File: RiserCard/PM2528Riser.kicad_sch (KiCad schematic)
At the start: 63 parts, among them K2 Conn_02x40_Odd_Even

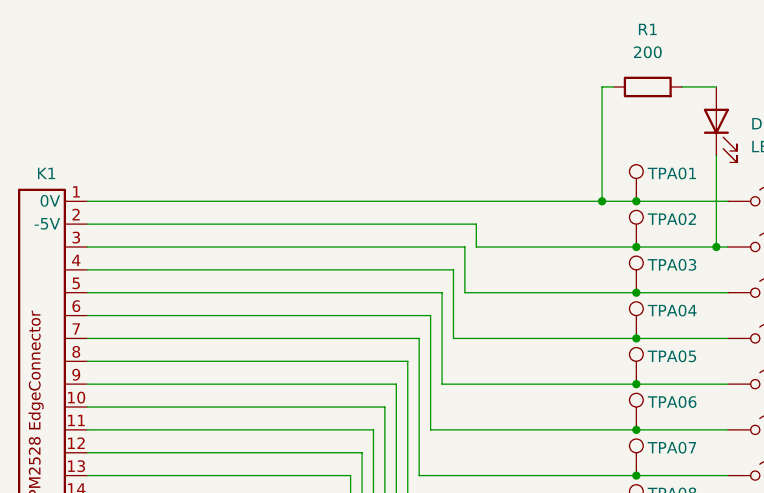
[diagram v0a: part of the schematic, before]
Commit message: Replaced testpins with testloops/beads
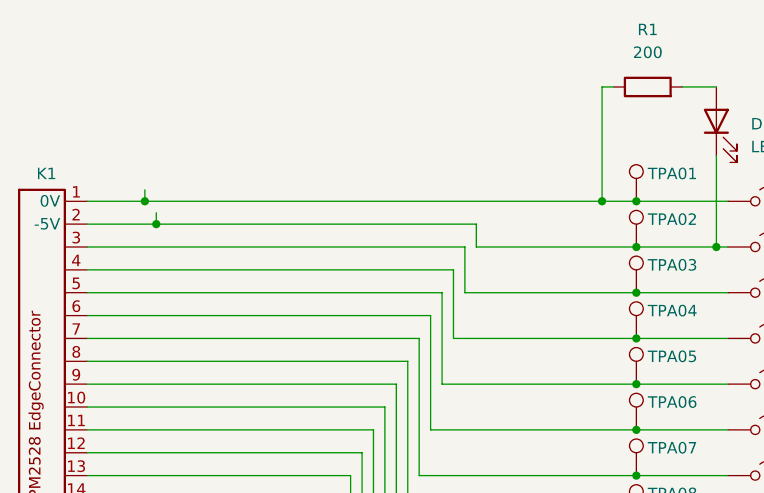
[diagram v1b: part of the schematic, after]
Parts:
- K1: symbol _PhilipsPM2528DMM:PCBEdge_Plugincard -> PM2528:PCBEdge_Plugincard
- TPB01, TPB02, TPB03, TPB04, TPB05, TPB06, TPB07, TPB08, TPB09, TPB10, TPB11, TPB12, TPB13, TPB14, TPB15, TPB16, TPB17, TPB18, TPB19: footprint Pin_D1.0mm_L10.0mm -> TestPoint:TestPoint_Loop_D1.80mm_Drill1.0mm_Beaded
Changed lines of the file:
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@@
 	(title_block
 		(title "PM2528 - Plugincard Riser")
-		(date "2024-08-17")
+		(date "2024-10-04")
 		(rev "2.0")
 		(company "D. Kupers")
@@
 	)
 	(junction
+		(at 91.44 54.61)
+		(diameter 0)
+		(color 0 0 0 0)
+	)
+	(junction
 		(at 185.42 102.87)
 		(diameter 0)
@@
 	)
 	(junction
+		(at 90.17 52.07)
+		(diameter 0)
+		(color 0 0 0 0)
+	)
+	(junction
 		(at 173.99 113.03)
 		(diameter 0)
@@
 	(wire
 		(pts
+			(xy 90.17 52.07) (xy 140.97 52.07)
+		)
+		(stroke
+			(width 0)
+			(type default)
+		)
+	)
+	(wire
+		(pts
 			(xy 125.73 62.23) (xy 144.78 62.23)
 		)
@@
 	(wire
 		(pts
-			(xy 83.82 52.07) (xy 140.97 52.07)
+			(xy 83.82 52.07) (xy 90.17 52.07)
 		)
 		(stroke
@@
 	(wire
 		(pts
+			(xy 90.17 50.8) (xy 90.17 52.07)
+		)
+		(stroke
+			(width 0)
+			(type default)
+		)
+	)
+	(wire
+		(pts
 			(xy 144.78 102.87) (xy 154.94 102.87)
 		)
@@
 	(wire
 		(pts
+			(xy 91.44 54.61) (xy 83.82 54.61)
+		)
+		(stroke
+			(width 0)
+			(type default)
+		)
+	)
+	(wire
+		(pts
 			(xy 144.78 62.23) (xy 154.94 62.23)
 		)
@@
 	(wire
 		(pts
+			(xy 91.44 53.34) (xy 91.44 54.61)
+		)
+		(stroke
+			(width 0)
+			(type default)
+		)
+	)
+	(wire
+		(pts
 			(xy 165.1 128.27) (xy 173.99 128.27)
 		)
@@
 	(wire
 		(pts
-			(xy 127 54.61) (xy 83.82 54.61)
+			(xy 127 54.61) (xy 91.44 54.61)
 		)
 		(stroke
@@
 		(length 2.54)
 		(shape round)
-		(at 91.44 54.61 0)
+		(at 91.44 53.34 0)
 		(fields_autoplaced yes)
 		(effects
@@
 		)
 		(property "Netclass" "Power"
-			(at 92.1385 52.07 0)
+			(at 92.1385 50.8 0)
 			(effects
 				(font
@@
 		(length 2.54)
 		(shape round)
-		(at 90.17 52.07 0)
+		(at 90.17 50.8 0)
 		(fields_autoplaced yes)
 		(effects
@@
 		)
 		(property "Netclass" "Power"
-			(at 90.8685 49.53 0)
+			(at 90.8685 48.26 0)
 			(effects
 				(font
@@
 			)
 		)
-		(property "Footprint" "Pin_D1.0mm_L10.0mm"
+		(property "Footprint" "TestPoint:TestPoint_Loop_D1.80mm_Drill1.0mm_Beaded"
 			(at 179.07 113.03 0)
 			(effects
@@
 			)
 		)
-		(property "Footprint" "Pin_D1.0mm_L10.0mm"
+		(property "Footprint" "TestPoint:TestPoint_Loop_D1.80mm_Drill1.0mm_Beaded"
 			(at 179.07 57.15 0)
 			(effects
@@
 			)
 		)
-		(property "Footprint" "Pin_D1.0mm_L10.0mm"
+		(property "Footprint" "TestPoint:TestPoint_Loop_D1.80mm_Drill1.0mm_Beaded"
 			(at 179.07 123.19 0)
 			(effects
@@
 			)
 		)
-		(property "Footprint" "Pin_D1.0mm_L10.0mm"
+		(property "Footprint" "TestPoint:TestPoint_Loop_D1.80mm_Drill1.0mm_Beaded"
 			(at 179.07 77.47 0)
 			(effects
@@
 			)
 		)
-		(property "Footprint" "Pin_D1.0mm_L10.0mm"
+		(property "Footprint" "TestPoint:TestPoint_Loop_D1.80mm_Drill1.0mm_Beaded"
 			(at 179.07 97.79 0)
 			(effects
@@
 			)
 		)
-		(property "Footprint" "Pin_D1.0mm_L10.0mm"
+		(property "Footprint" "TestPoint:TestPoint_Loop_D1.80mm_Drill1.0mm_Beaded"
 			(at 179.07 87.63 0)
 			(effects
@@
 			)
 		)
-		(property "Footprint" "Pin_D1.0mm_L10.0mm"
+		(property "Footprint" "TestPoint:TestPoint_Loop_D1.80mm_Drill1.0mm_Beaded"
 			(at 179.07 143.51 0)
 			(effects
@@
 			)
 		)
-		(property "Footprint" "Pin_D1.0mm_L10.0mm"
+		(property "Footprint" "TestPoint:TestPoint_Loop_D1.80mm_Drill1.0mm_Beaded"
 			(at 179.07 107.95 0)
 			(effects
@@
 	)
 	(symbol
-		(lib_id "_PhilipsPM2528DMM:PCBEdge_Plugincard")
+		(lib_id "PM2528:PCBEdge_Plugincard")
 		(at 78.74 74.93 0)
 		(unit 1)
@@
 			)
 		)
-		(property "Footprint" "Pin_D1.0mm_L10.0mm"
+		(property "Footprint" "TestPoint:TestPoint_Loop_D1.80mm_Drill1.0mm_Beaded"
 			(at 179.07 138.43 0)
 			(effects
@@
 			)
 		)
-		(property "Footprint" "Pin_D1.0mm_L10.0mm"
+		(property "Footprint" "TestPoint:TestPoint_Loop_D1.80mm_Drill1.0mm_Beaded"
 			(at 179.07 102.87 0)
 			(effects
@@
 			)
 		)
-		(property "Footprint" "Pin_D1.0mm_L10.0mm"
+		(property "Footprint" "TestPoint:TestPoint_Loop_D1.80mm_Drill1.0mm_Beaded"
 			(at 179.07 118.11 0)
 			(effects
@@
 			)
 		)
-		(property "Footprint" "Pin_D1.0mm_L10.0mm"
+		(property "Footprint" "TestPoint:TestPoint_Loop_D1.80mm_Drill1.0mm_Beaded"
 			(at 179.07 128.27 0)
 			(effects
@@
 			)
 		)
-		(property "Footprint" "Pin_D1.0mm_L10.0mm"
+		(property "Footprint" "TestPoint:TestPoint_Loop_D1.80mm_Drill1.0mm_Beaded"
 			(at 179.07 62.23 0)
 			(effects
@@
 			)
 		)
-		(property "Footprint" "Pin_D1.0mm_L10.0mm"
+		(property "Footprint" "TestPoint:TestPoint_Loop_D1.80mm_Drill1.0mm_Beaded"
 			(at 179.07 133.35 0)
 			(effects
@@
 			)
 		)
-		(property "Footprint" "Pin_D1.0mm_L10.0mm"
+		(property "Footprint" "TestPoint:TestPoint_Loop_D1.80mm_Drill1.0mm_Beaded"
 			(at 179.07 67.31 0)
 			(effects
@@
 			)
 		)
-		(property "Footprint" "Pin_D1.0mm_L10.0mm"
+		(property "Footprint" "TestPoint:TestPoint_Loop_D1.80mm_Drill1.0mm_Beaded"
 			(at 179.07 82.55 0)
 			(effects
@@
 			)
 		)
-		(property "Footprint" "Pin_D1.0mm_L10.0mm"
+		(property "Footprint" "TestPoint:TestPoint_Loop_D1.80mm_Drill1.0mm_Beaded"
 			(at 179.07 52.07 0)
 			(effects
@@
 			)
 		)
-		(property "Footprint" "Pin_D1.0mm_L10.0mm"
+		(property "Footprint" "TestPoint:TestPoint_Loop_D1.80mm_Drill1.0mm_Beaded"
 			(at 179.07 92.71 0)
 			(effects
@@
 			)
 		)
-		(property "Footprint" "Pin_D1.0mm_L10.0mm"
+		(property "Footprint" "TestPoint:TestPoint_Loop_D1.80mm_Drill1.0mm_Beaded"
 			(at 179.07 72.39 0)
 			(effects

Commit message: Updates, add N25
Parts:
- K1: footprint Philips_PM2528:PM2528_RiserCardConnector -> PM2528:PM2528_RiserCardConnector
- K2: footprint Philips_PM2528:CONN EDGE DUAL FMALE 80POS 0.100 -> PM2528:CONN EDGE DUAL FMALE 80POS 0.100
- TPA01, TPA02, TPA03, TPA04, TPA05, TPA06, TPA07, TPA08, TPA09, TPA10, TPA11, TPA12, TPA13, TPA14, TPA15, TPA16, TPA17, TPA18, TPA19: footprint Pin_D1.0mm_L10.0mm -> Connector_Pin:Pin_D1.0mm_L10.0mm
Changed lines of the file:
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@@
 (kicad_sch
-	(version 20231120)
+	(version 20250114)
 	(generator "eeschema")
-	(generator_version "8.0")
+	(generator_version "9.0")
 	(paper "A4")
 	(title_block
@@
 	)
 	(junction
-		(at 91.44 54.61)
-		(diameter 0)
-		(color 0 0 0 0)
-	)
-	(junction
 		(at 185.42 102.87)
 		(diameter 0)
@@
 	)
 	(junction
-		(at 90.17 52.07)
-		(diameter 0)
-		(color 0 0 0 0)
-	)
-	(junction
 		(at 173.99 113.03)
 		(diameter 0)
@@
 	(wire
 		(pts
-			(xy 90.17 52.07) (xy 140.97 52.07)
+			(xy 83.82 52.07) (xy 140.97 52.07)
 		)
 		(stroke
@@
 	(wire
 		(pts
-			(xy 83.82 52.07) (xy 90.17 52.07)
-		)
-		(stroke
-			(width 0)
-			(type default)
-		)
-	)
-	(wire
-		(pts
 			(xy 165.1 57.15) (xy 170.18 57.15)
 		)
@@
 	(wire
 		(pts
-			(xy 90.17 50.8) (xy 90.17 52.07)
-		)
-		(stroke
-			(width 0)
-			(type default)
-		)
-	)
-	(wire
-		(pts
 			(xy 144.78 102.87) (xy 154.94 102.87)
 		)
@@
 	(wire
 		(pts
-			(xy 91.44 54.61) (xy 83.82 54.61)
+			(xy 83.82 54.61) (xy 127 54.61)
 		)
 		(stroke
@@
 	(wire
 		(pts
-			(xy 91.44 53.34) (xy 91.44 54.61)
-		)
-		(stroke
-			(width 0)
-			(type default)
-		)
-	)
-	(wire
-		(pts
 			(xy 165.1 128.27) (xy 173.99 128.27)
 		)
@@
 	(wire
 		(pts
-			(xy 127 54.61) (xy 91.44 54.61)
-		)
-		(stroke
-			(width 0)
-			(type default)
-		)
-	)
-	(wire
-		(pts
 			(xy 120.65 82.55) (xy 144.78 82.55)
 		)
@@
 		)
 	)
-	(netclass_flag ""
-		(length 2.54)
-		(shape round)
-		(at 184.15 52.07 0)
-		(fields_autoplaced yes)
-		(effects
-			(font
-				(size 1.27 1.27)
-			)
-			(justify left bottom)
-		)
-		(property "Netclass" "Power"
-			(at 184.8485 49.53 0)
-			(effects
-				(font
-					(size 1.27 1.27)
-					(italic yes)
-				)
-				(justify left)
-			)
-		)
-	)
-	(netclass_flag ""
-		(length 2.54)
-		(shape round)
-		(at 91.44 53.34 0)
-		(fields_autoplaced yes)
-		(effects
-			(font
-				(size 1.27 1.27)
-			)
-			(justify left bottom)
-		)
-		(property "Netclass" "Power"
-			(at 92.1385 50.8 0)
-			(effects
-				(font
-					(size 1.27 1.27)
-					(italic yes)
-				)
-				(justify left)
-			)
-		)
-	)
-	(netclass_flag ""
-		(length 2.54)
-		(shape round)
-		(at 90.17 50.8 0)
-		(fields_autoplaced yes)
-		(effects
-			(font
-				(size 1.27 1.27)
-			)
-			(justify left bottom)
-		)
-		(property "Netclass" "Power"
-			(at 90.8685 48.26 0)
-			(effects
-				(font
-					(size 1.27 1.27)
-					(italic yes)
-				)
-				(justify left)
-			)
-		)
-	)
-	(netclass_flag ""
-		(length 2.54)
-		(shape round)
-		(at 184.15 57.15 0)
-		(fields_autoplaced yes)
-		(effects
-			(font
-				(size 1.27 1.27)
-			)
-			(justify left bottom)
-		)
-		(property "Netclass" "Power"
-			(at 184.8485 54.61 0)
-			(effects
-				(font
-					(size 1.27 1.27)
-					(italic yes)
-				)
-				(justify left)
-			)
-		)
-	)
 	(symbol
 		(lib_id "Connector:TestPoint")
@@
 			)
 		)
-		(property "Footprint" "Pin_D1.0mm_L10.0mm"
+		(property "Footprint" "Connector_Pin:Pin_D1.0mm_L10.0mm"
 			(at 149.86 138.43 0)
 			(effects
@@
 			)
 		)
-		(property "Footprint" "Pin_D1.0mm_L10.0mm"
+		(property "Footprint" "Connector_Pin:Pin_D1.0mm_L10.0mm"
 			(at 149.86 77.47 0)
 			(effects
@@
 			)
 		)
-		(property "Footprint" "Pin_D1.0mm_L10.0mm"
+		(property "Footprint" "Connector_Pin:Pin_D1.0mm_L10.0mm"
 			(at 149.86 72.39 0)
 			(effects
@@
 			)
 		)
-		(property "Footprint" "Pin_D1.0mm_L10.0mm"
+		(property "Footprint" "Connector_Pin:Pin_D1.0mm_L10.0mm"
 			(at 149.86 123.19 0)
 			(effects
@@
 			)
 		)
-		(property "Footprint" "Pin_D1.0mm_L10.0mm"
+		(property "Footprint" "Connector_Pin:Pin_D1.0mm_L10.0mm"
 			(at 149.86 82.55 0)
 			(effects
@@
 			)
 		)
-		(property "Footprint" "Pin_D1.0mm_L10.0mm"
+		(property "Footprint" "Connector_Pin:Pin_D1.0mm_L10.0mm"
 			(at 149.86 52.07 0)
 			(effects
@@
 			)
 		)
-		(property "Footprint" "Pin_D1.0mm_L10.0mm"
+		(property "Footprint" "Connector_Pin:Pin_D1.0mm_L10.0mm"
 			(at 149.86 143.51 0)
 			(effects
@@
 			)
 		)
+		(property "Sim.Pins" "1=K 2=A"
+			(at 170.18 43.18 0)
+			(effects
+				(font
+					(size 1.27 1.27)
+				)
+				(hide yes)
+			)
+		)
 		(pin "2"
 		)
@@
 			)
 		)
-		(property "Footprint" "Pin_D1.0mm_L10.0mm"
+		(property "Footprint" "Connector_Pin:Pin_D1.0mm_L10.0mm"
 			(at 149.86 97.79 0)
 			(effects
@@
 			)
 		)
-		(property "Footprint" "Philips_PM2528:PM2528_RiserCardConnector"
+		(property "Footprint" "PM2528:PM2528_RiserCardConnector"
 			(at 90.17 52.07 0)
 			(effects
@@
 			)
 		)
-		(property "Footprint" "Philips_PM2528:CONN EDGE DUAL FMALE 80POS 0.100"
+		(property "Footprint" "PM2528:CONN EDGE DUAL FMALE 80POS 0.100"
 			(at 190.5 97.79 0)
 			(effects
@@
 			)
 		)
+		(property "Sim.Pins" "1=K 2=A"
+			(at 153.67 43.18 0)
+			(effects
+				(font
+					(size 1.27 1.27)
+				)
+				(hide yes)
+			)
+		)
 		(pin "2"
 		)
@@
 			)
 		)
-		(property "Footprint" "Pin_D1.0mm_L10.0mm"
+		(property "Footprint" "Connector_Pin:Pin_D1.0mm_L10.0mm"
 			(at 149.86 107.95 0)
 			(effects
@@
 			)
 		)
-		(property "Footprint" "Pin_D1.0mm_L10.0mm"
+		(property "Footprint" "Connector_Pin:Pin_D1.0mm_L10.0mm"
 			(at 149.86 57.15 0)
 			(effects
@@
 			)
 		)
-		(property "Footprint" "Pin_D1.0mm_L10.0mm"
+		(property "Footprint" "Connector_Pin:Pin_D1.0mm_L10.0mm"
 			(at 149.86 133.35 0)
 			(effects
@@
 			)
 		)
-		(property "Footprint" "Pin_D1.0mm_L10.0mm"
+		(property "Footprint" "Connector_Pin:Pin_D1.0mm_L10.0mm"
 			(at 149.86 67.31 0)
 			(effects
@@
 			)
 		)
-		(property "Footprint" "Pin_D1.0mm_L10.0mm"
+		(property "Footprint" "Connector_Pin:Pin_D1.0mm_L10.0mm"
 			(at 149.86 92.71 0)
 			(effects
@@
 			)
 		)
-		(property "Footprint" "Pin_D1.0mm_L10.0mm"
+		(property "Footprint" "Connector_Pin:Pin_D1.0mm_L10.0mm"
 			(at 149.86 62.23 0)
 			(effects
@@
 			)
 		)
-		(property "Footprint" "Pin_D1.0mm_L10.0mm"
+		(property "Footprint" "Connector_Pin:Pin_D1.0mm_L10.0mm"
 			(at 149.86 113.03 0)
 			(effects
@@
 			)
 		)
-		(property "Footprint" "Pin_D1.0mm_L10.0mm"
+		(property "Footprint" "Connector_Pin:Pin_D1.0mm_L10.0mm"
 			(at 149.86 102.87 0)
 			(effects
@@
 			)
 		)
-		(property "Footprint" "Pin_D1.0mm_L10.0mm"
+		(property "Footprint" "Connector_Pin:Pin_D1.0mm_L10.0mm"
 			(at 149.86 128.27 0)
 			(effects
@@
 			)
 		)
-		(property "Footprint" "Pin_D1.0mm_L10.0mm"
+		(property "Footprint" "Connector_Pin:Pin_D1.0mm_L10.0mm"
 			(at 149.86 118.11 0)
 			(effects
@@
 			)
 		)
-		(property "Footprint" "Pin_D1.0mm_L10.0mm"
+		(property "Footprint" "Connector_Pin:Pin_D1.0mm_L10.0mm"
 			(at 149.86 87.63 0)
 			(effects
@@
 		)
 	)
+	(embedded_fonts no)
 )
